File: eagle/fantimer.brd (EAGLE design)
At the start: 58 x 78 mm, 18 parts, among them IC1 PIC10F220, K1 PB2032-ND, Q1 2N7000-G, U1 IRM-01-5, X1 732-10957-ND

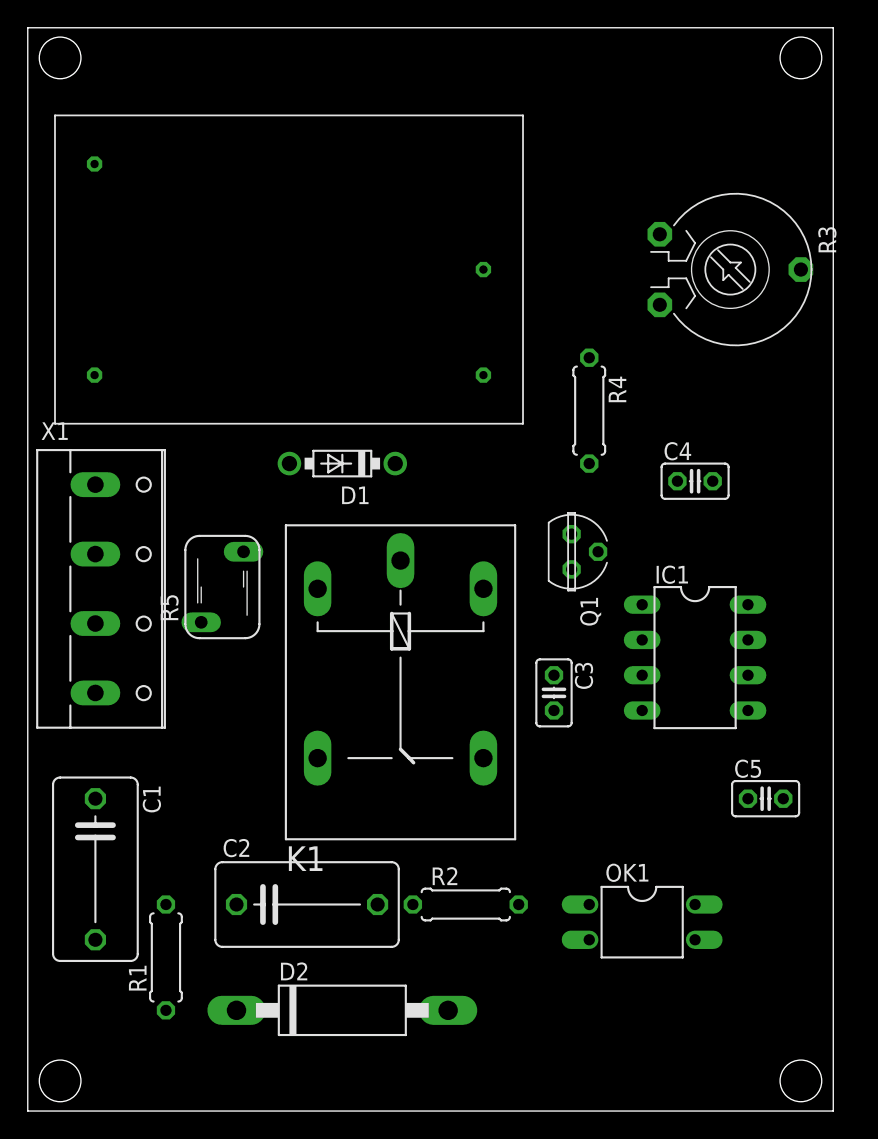
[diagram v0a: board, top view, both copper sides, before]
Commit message: - Fix for backward PSU - CPTC fuse added on light line - Filament fuse added on AC/L line - Drop analysis (that goes in the report)
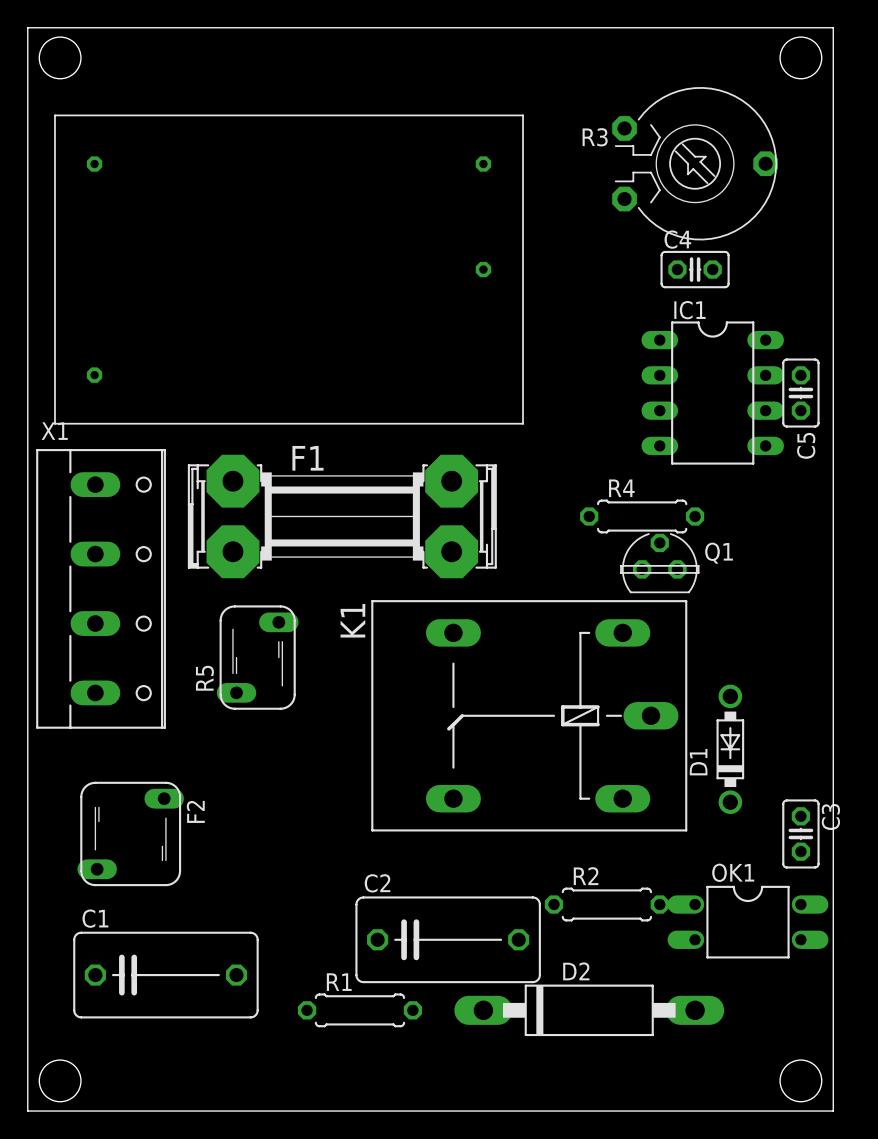
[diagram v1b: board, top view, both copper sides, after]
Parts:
- added F1: 5MF 5-R, fuse:SHK20Q
- added F2: CMF-RL35-0, varistor:S05K460
- moved D1 34.7 mm to (48.3, 18.8), turned to 90 degrees
- moved C5 29.3 mm to (53.3, 44.5), turned to 90 degrees
- moved C3 20.5 mm to (53.3, 12.7)
- moved IC1 19.1 mm to (47.0, 44.5)
- moved D2 17.8 mm to (38.1, 0.00)
- moved C4 15.2 mm to (45.7, 53.3)
- moved R1 14.5 mm to (21.6, 0.00), turned to 0 degrees
- moved C2 10.5 mm to (27.9, 5.08)
- moved R2 10.2 mm to (39.4, 7.62)
- moved C1 9.16 mm to (7.62, 2.54), turned to 0 degrees
- moved K1 8.67 mm to (33.0, 21.2), turned to 180 degrees
- moved R4 8.52 mm to (41.9, 35.6), turned to 0 degrees
- moved R3 8.03 mm to (45.7, 61.0)
- moved OK1 7.62 mm to (49.5, 6.35)
- moved Q1 6.48 mm to (43.2, 31.8), turned to 0 degrees
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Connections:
- new net AC/L_FUSE: F1.1A, X1.2
- new net LIGHT_FUSE: F2.1, X1.4
- net AC/L: now also F1.2A; no longer X1.2
- net LIVE_LIGHT: now also F2.2; no longer X1.4

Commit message: Clean up for report; add high-v line
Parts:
- moved C3 6.35 mm to (49.5, 17.8), turned to 0 degrees
- moved D1 5.80 mm to (43.2, 21.6)
- moved Q1 5.68 mm to (48.3, 29.2), turned to 180 degrees
- moved R4 5.08 mm to (47.0, 35.6), turned to 180 degrees
- moved K1 5.08 mm to (27.9, 21.2)
- moved C2 3.59 mm to (25.4, 7.62)
- moved R5 2.54 mm to (11.7, 25.4)
- moved C1 2.54 mm to (5.08, 2.54)
- moved D2 2.54 mm to (35.6, 0.00)
- moved F1 2.54 mm to (22.9, 35.6)
- moved R1 2.54 mm to (19.1, 0.00)
- moved C4 1.27 mm to (44.5, 53.3)
- moved F2 0.18 mm to (4.95, 12.8)

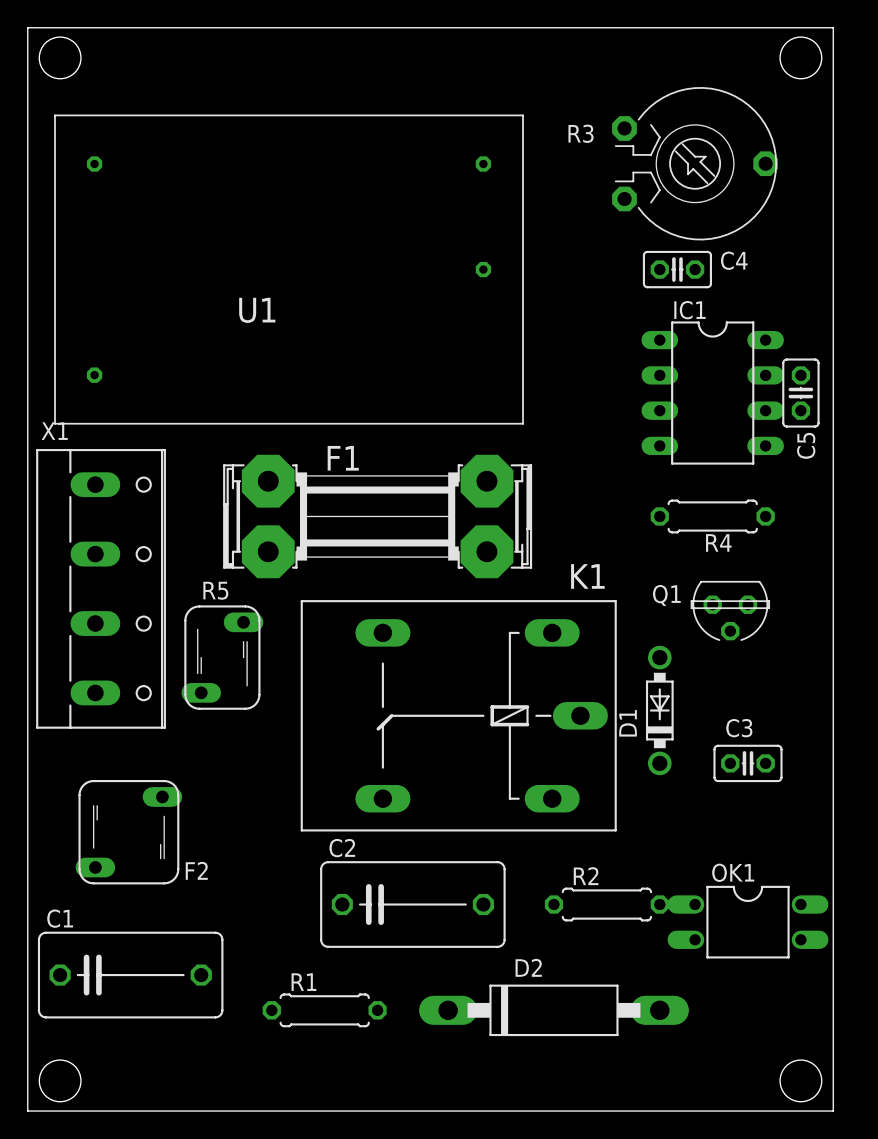
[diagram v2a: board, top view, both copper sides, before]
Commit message: Rearrange board taking advantage of ground buses. CPTC is narrower than predicted.
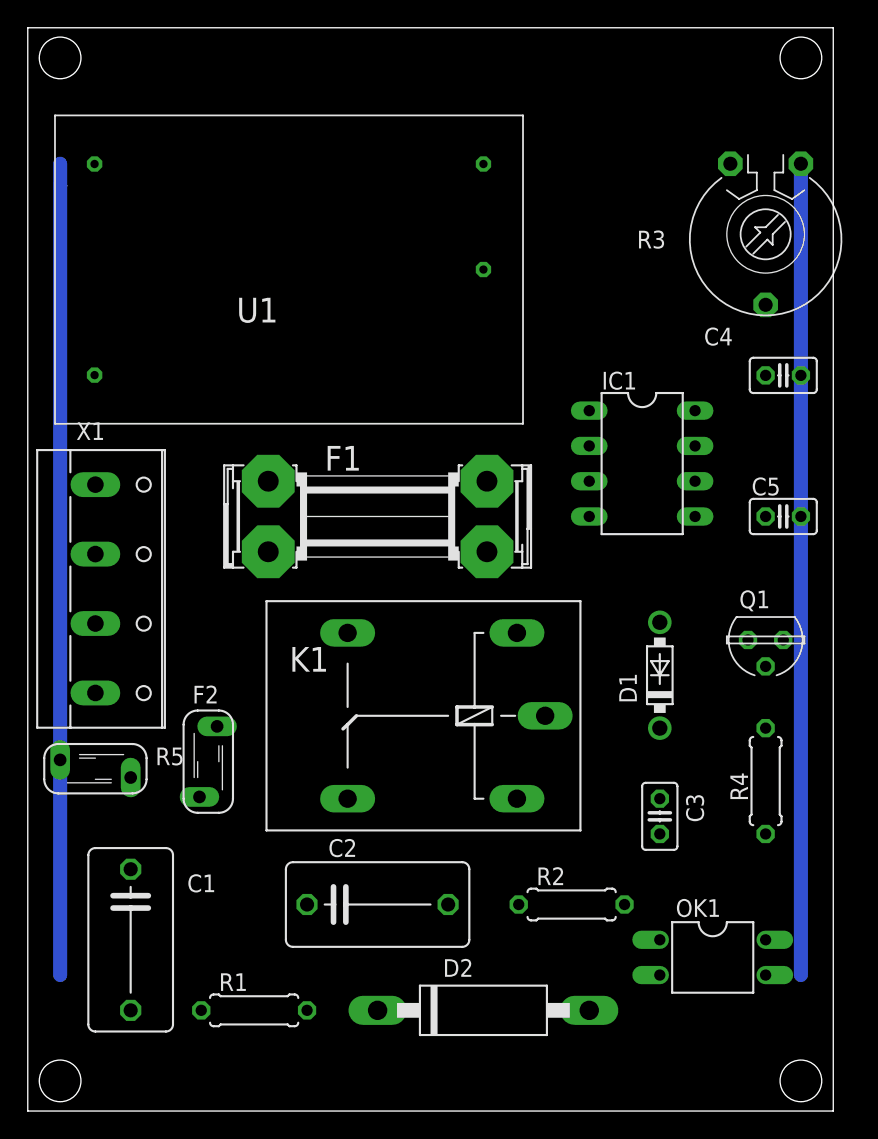
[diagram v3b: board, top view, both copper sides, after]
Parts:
- F2: device varistor:S05K460 -> varistor:S05K11
- R5: device varistor:S05K300 -> varistor:S05K11
- moved R4 19.4 mm to (50.8, 16.5), turned to 90 degrees
- moved R5 12.2 mm to (2.54, 17.4), turned to 90 degrees
- moved C4 10.8 mm to (52.1, 45.7)
- moved C5 8.98 mm to (52.1, 35.6), turned to 0 degrees
- moved F2 7.65 mm to (10.7, 17.9)
- moved C3 7.41 mm to (43.2, 14.0), turned to 270 degrees
- moved IC1 7.18 mm to (41.9, 39.4)
- moved R3 7.18 mm to (50.8, 55.9), turned to 180 degrees
- moved D2 5.08 mm to (30.5, 0.00)
- moved R1 5.08 mm to (14.0, 0.00)
- moved OK1 3.59 mm to (47.0, 3.81)
- moved Q1 3.59 mm to (50.8, 26.7)
- moved K1 2.54 mm to (25.4, 21.2)
- moved C1 2.54 mm to (5.08, 5.08), turned to 270 degrees
- moved C2 2.54 mm to (22.9, 7.62)
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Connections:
- net +5V: now also R3.2; no longer R3.1
- net GND: now also R3.1; no longer R3.2
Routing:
- net GND: track 0.00 -> 58.4 mm
- net AC/N: track 0.00 -> 58.4 mm

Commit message: Move TVS closer to neut bus
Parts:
- moved D2 23.0 mm to (7.62, 2.54), turned to 180 degrees
- moved C2 9.16 mm to (30.5, 2.54)
- moved R1 8.98 mm to (20.3, 6.35), turned to 270 degrees
- moved C1 7.18 mm to (10.2, 10.2), turned to 0 degrees
- moved F2 2.54 mm to (10.7, 20.4)
- moved R2 2.54 mm to (39.4, 7.62)
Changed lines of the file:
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@@
 <attribute name="VALUE" x="44.069" y="-0.381" size="1.27" layer="27" ratio="10"/>
 </element>
-<element name="R2" library="resistor" library_urn="urn:adsk.eagle:library:348" package="0207/7" package3d_urn="urn:adsk.eagle:package:23493/1" value="1.6k" x="36.83" y="7.62">
-<attribute name="NAME" x="34.29" y="9.017" size="1.27" layer="25" ratio="10"/>
-<attribute name="VALUE" x="34.544" y="7.0612" size="1.27" layer="27" ratio="10"/>
+<element name="R2" library="resistor" library_urn="urn:adsk.eagle:library:348" package="0207/7" package3d_urn="urn:adsk.eagle:package:23493/1" value="1.6k" x="39.37" y="7.62">
+<attribute name="NAME" x="36.83" y="9.017" size="1.27" layer="25" ratio="10"/>
+<attribute name="VALUE" x="37.084" y="7.0612" size="1.27" layer="27" ratio="10"/>
 </element>
-<element name="D2" library="diode" library_urn="urn:adsk.eagle:library:210" package="CB417-15" package3d_urn="urn:adsk.eagle:package:43349/1" value="P6KE91CA" x="30.48" y="0">
-<attribute name="NAME" x="27.559" y="2.413" size="1.27" layer="25" ratio="10"/>
-<attribute name="VALUE" x="27.686" y="-1.397" size="1.27" layer="27" ratio="10"/>
+<element name="D2" library="diode" library_urn="urn:adsk.eagle:library:210" package="CB417-15" package3d_urn="urn:adsk.eagle:package:43349/1" value="P6KE91CA" x="7.62" y="2.54" rot="R180">
+<attribute name="NAME" x="10.541" y="0.127" size="1.27" layer="25" ratio="10" rot="R180"/>
+<attribute name="VALUE" x="10.414" y="3.937" size="1.27" layer="27" ratio="10" rot="R180"/>
 </element>
-<element name="C1" library="rcl" library_urn="urn:adsk.eagle:library:334" package="C102-064X133" package3d_urn="urn:adsk.eagle:package:23653/1" value="330nF" x="5.08" y="5.08" rot="R270">
-<attribute name="NAME" x="9.144" y="8.509" size="1.27" layer="25" ratio="10"/>
-<attribute name="SPICEPREFIX" value="C" x="5.08" y="5.08" size="1.778" layer="27" rot="R270" display="off"/>
-<attribute name="VALUE" x="3.048" y="6.604" size="1.27" layer="27" ratio="10" rot="R270"/>
+<element name="C1" library="rcl" library_urn="urn:adsk.eagle:library:334" package="C102-064X133" package3d_urn="urn:adsk.eagle:package:23653/1" value="330nF" x="10.16" y="10.16">
+<attribute name="NAME" x="6.096" y="6.731" size="1.27" layer="25" ratio="10" rot="R180"/>
+<attribute name="SPICEPREFIX" value="C" x="10.16" y="10.16" size="1.778" layer="27" display="off"/>
+<attribute name="VALUE" x="8.636" y="8.128" size="1.27" layer="27" ratio="10"/>
 </element>
-<element name="C2" library="rcl" library_urn="urn:adsk.eagle:library:334" package="C102-064X133" package3d_urn="urn:adsk.eagle:package:23653/1" value="330nF" x="22.86" y="7.62">
-<attribute name="NAME" x="19.304" y="11.049" size="1.27" layer="25" ratio="10"/>
-<attribute name="SPICEPREFIX" value="C" x="22.86" y="7.62" size="1.778" layer="27" display="off"/>
-<attribute name="VALUE" x="21.336" y="5.588" size="1.27" layer="27" ratio="10"/>
+<element name="C2" library="rcl" library_urn="urn:adsk.eagle:library:334" package="C102-064X133" package3d_urn="urn:adsk.eagle:package:23653/1" value="330nF" x="30.48" y="2.54">
+<attribute name="NAME" x="26.924" y="5.969" size="1.27" layer="25" ratio="10"/>
+<attribute name="SPICEPREFIX" value="C" x="30.48" y="2.54" size="1.778" layer="27" display="off"/>
+<attribute name="VALUE" x="28.956" y="0.508" size="1.27" layer="27" ratio="10"/>
 </element>
-<element name="R1" library="resistor" library_urn="urn:adsk.eagle:library:348" package="0207/7" package3d_urn="urn:adsk.eagle:package:23493/1" value="1.6k" x="13.97" y="0">
-<attribute name="NAME" x="11.43" y="1.397" size="1.27" layer="25" ratio="10"/>
-<attribute name="VALUE" x="11.684" y="-0.5588" size="1.27" layer="27" ratio="10"/>
+<element name="R1" library="resistor" library_urn="urn:adsk.eagle:library:348" package="0207/7" package3d_urn="urn:adsk.eagle:package:23493/1" value="1.6k" x="20.32" y="6.35" rot="R270">
+<attribute name="NAME" x="21.717" y="8.89" size="1.27" layer="25" ratio="10" rot="R270"/>
+<attribute name="VALUE" x="19.7612" y="8.636" size="1.27" layer="27" ratio="10" rot="R270"/>
 </element>
 <element name="R3" library="rcl" library_urn="urn:adsk.eagle:library:334" package="PT-10" package3d_urn="urn:adsk.eagle:package:23786/1" value="4.7k" x="50.8" y="55.88" rot="R180">
@@
 </element>
 <element name="R5" library="varistor" library_urn="urn:adsk.eagle:library:410" package="S05K11" package3d_urn="urn:adsk.eagle:package:30524/1" value="MOV-07D201K" x="2.54" y="17.399" rot="R90">
-<attribute name="NAME" x="6.858" y="17.653" size="1.27" layer="25" ratio="10"/>
+<attribute name="NAME" x="6.858" y="15.113" size="1.27" layer="25" ratio="10"/>
 <attribute name="VALUE" x="-0.381" y="13.462" size="1.27" layer="27" ratio="10"/>
 </element>
@@
 <attribute name="VALUE" x="21.59" y="30.48" size="1.778" layer="27" ratio="10"/>
 </element>
-<element name="F2" library="varistor" library_urn="urn:adsk.eagle:library:410" package="S05K11" package3d_urn="urn:adsk.eagle:package:30524/1" value="CMF-RL35-0" x="10.668" y="17.907" rot="R180">
-<attribute name="NAME" x="9.525" y="22.098" size="1.27" layer="25" ratio="10"/>
-<attribute name="VALUE" x="13.716" y="15.24" size="1.27" layer="27" ratio="10" rot="R90"/>
+<element name="F2" library="varistor" library_urn="urn:adsk.eagle:library:410" package="S05K11" package3d_urn="urn:adsk.eagle:package:30524/1" value="CMF-RL35-0" x="10.668" y="20.447" rot="R180">
+<attribute name="NAME" x="9.525" y="24.638" size="1.27" layer="25" ratio="10"/>
+<attribute name="VALUE" x="13.716" y="17.78" size="1.27" layer="27" ratio="10" rot="R90"/>
 </element>
 </elements>
@@
 <contactref element="D2" pad="A"/>
 <contactref element="R5" pad="2"/>
-<wire x1="0" y1="59.3852" x2="0" y2="59.4106" width="1.016" layer="16"/>
-<wire x1="0" y1="59.4106" x2="0" y2="60.96" width="1.016" layer="16"/>
-<wire x1="0" y1="59.3598" x2="0" y2="59.3852" width="1.016" layer="16"/>
-<wire x1="0" y1="59.3598" x2="0" y2="59.3344" width="1.016" layer="16"/>
-<wire x1="0" y1="59.3344" x2="0" y2="2.54" width="1.016" layer="16"/>
+<wire x1="0" y1="60.96" x2="0" y2="2.54" width="1.016" layer="16"/>
 <wire x1="0" y1="60.96" x2="2.48" y2="60.94" width="0" layer="19" extent="16-16"/>
-<wire x1="0" y1="18.034" x2="0" y2="2.54" width="0" layer="19" extent="16-16"/>
+<wire x1="0" y1="18.034" x2="0" y2="2.54" width="0" layer="19" extent="1-1"/>
 <wire x1="2.54" y1="37.853" x2="0" y2="18.034" width="0" layer="19" extent="1-1"/>
-<wire x1="38.1" y1="0" x2="0" y2="2.54" width="0" layer="19" extent="16-16"/>
-<wire x1="43.18" y1="2.54" x2="38.1" y2="0" width="0" layer="19" extent="1-1"/>
+<wire x1="43.18" y1="2.54" x2="0" y2="2.54" width="0" layer="19" extent="1-1"/>
 </signal>
 <signal name="AC/L">
@@
 <contactref element="C1" pad="1"/>
 <contactref element="F2" pad="2"/>
-<wire x1="5.08" y1="10.16" x2="10.033" y2="15.367" width="0" layer="19" extent="1-1"/>
+<wire x1="5.08" y1="10.16" x2="10.033" y2="17.907" width="0" layer="19" extent="1-1"/>
 </signal>
 <signal name="FAN">
@@
 <contactref element="R2" pad="2"/>
 <contactref element="OK1" pad="1"/>
-<wire x1="43.18" y1="5.08" x2="40.64" y2="7.62" width="0" layer="19" extent="1-1"/>
+<wire x1="43.18" y1="5.08" x2="43.18" y2="7.62" width="0" layer="19" extent="1-1"/>
 </signal>
 <signal name="VZ">
@@
 <contactref element="C2" pad="1"/>
 <contactref element="R1" pad="2"/>
-<wire x1="17.78" y1="0" x2="17.78" y2="7.62" width="0" layer="19" extent="1-1"/>
-<wire x1="22.86" y1="0" x2="17.78" y2="0" width="0" layer="19" extent="1-1"/>
+<wire x1="20.32" y1="2.54" x2="25.4" y2="2.54" width="0" layer="19" extent="1-1"/>
+<wire x1="15.24" y1="2.54" x2="20.32" y2="2.54" width="0" layer="19" extent="1-1"/>
 </signal>
 <signal name="VRC2">
 <contactref element="C2" pad="2"/>
 <contactref element="R2" pad="1"/>
-<wire x1="27.94" y1="7.62" x2="33.02" y2="7.62" width="0" layer="19" extent="1-1"/>
+<wire x1="35.56" y1="2.54" x2="35.56" y2="7.62" width="0" layer="19" extent="1-1"/>
 </signal>
 <signal name="VRC1">
 <contactref element="C1" pad="2"/>
 <contactref element="R1" pad="1"/>
-<wire x1="5.08" y1="0" x2="10.16" y2="0" width="0" layer="19" extent="1-1"/>
+<wire x1="15.24" y1="10.16" x2="20.32" y2="10.16" width="0" layer="19" extent="1-1"/>
 </signal>
 <signal name="TIMER1">
@@
 <contactref element="X1" pad="4"/>
 <contactref element="F2" pad="1"/>
-<wire x1="2.54" y1="22.853" x2="11.303" y2="20.447" width="0" layer="19" extent="1-1"/>
+<wire x1="2.54" y1="22.853" x2="11.303" y2="22.987" width="0" layer="19" extent="1-1"/>
 </signal>
 </signals>
